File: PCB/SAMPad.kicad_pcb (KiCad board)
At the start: 2 copper layers, 73.2 x 116 mm, 162 parts, among them P1 USB_CONN, P1_2 USB_CONN, P4 CONN_6, P5 CONN_6, P6 ISP6, U1 ATMEGA32U4, U3 IP4234CZ6, U4 AP3417C, U5 PAM2804, X1 CRYSTAL

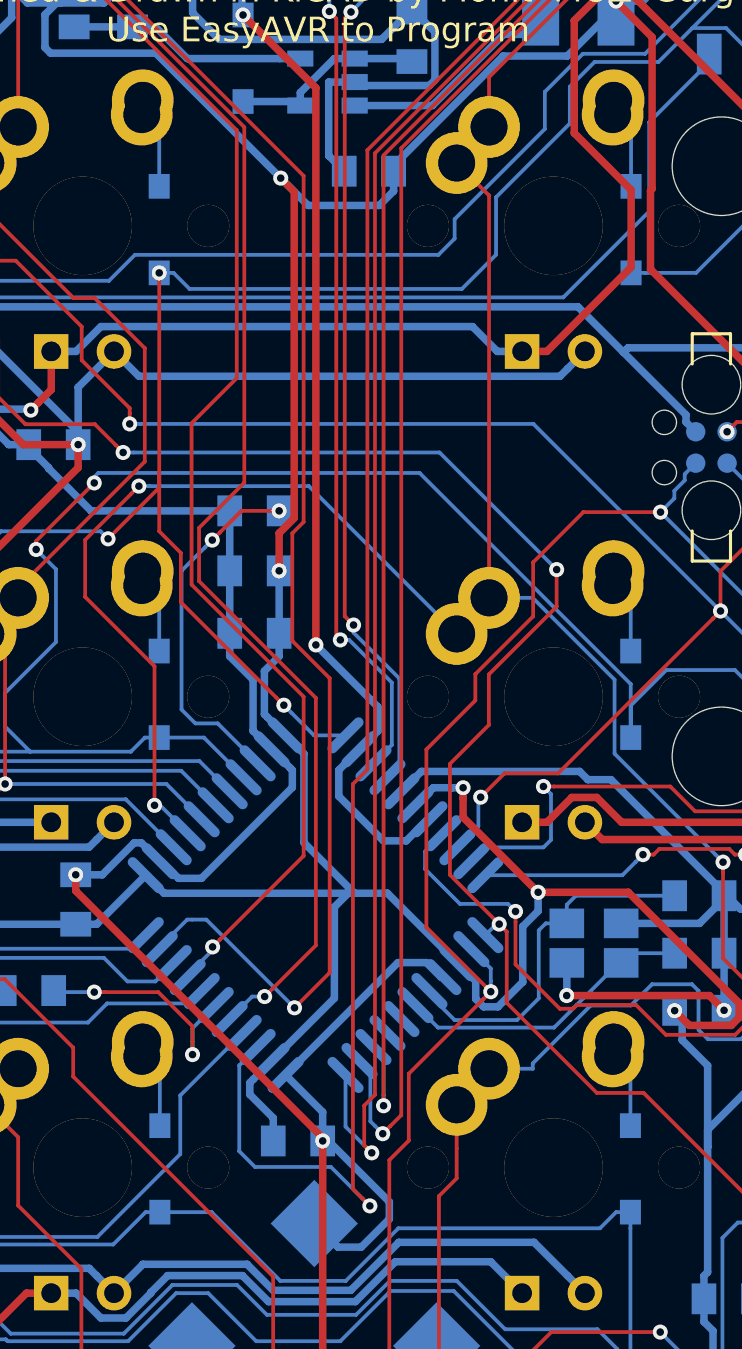
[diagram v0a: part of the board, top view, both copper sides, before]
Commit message: Fix Possible UVCC error
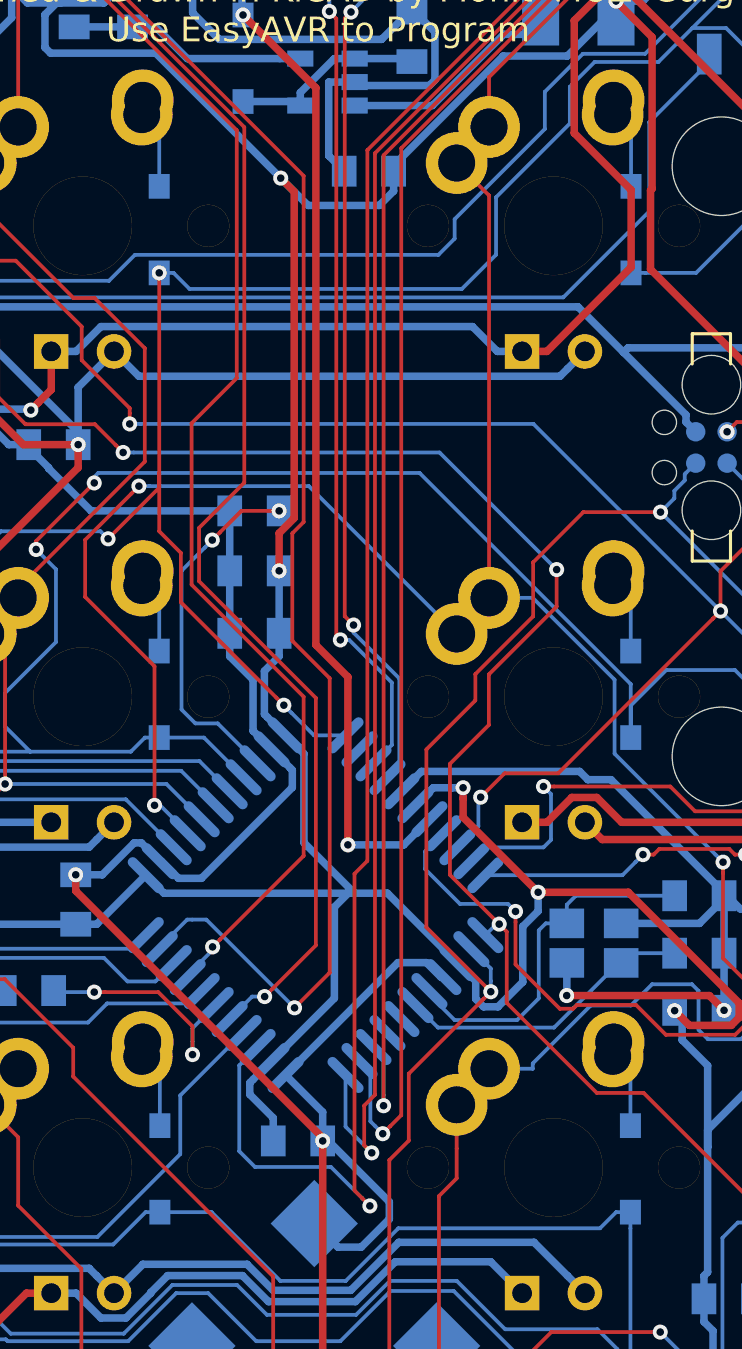
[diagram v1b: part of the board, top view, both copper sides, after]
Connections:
- U1 pad 2: /mcu/VUSB -> (no net)
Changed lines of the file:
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@@
 (kicad_pcb (version 4) (host pcbnew 4.0.1-stable)
   (general
-    (links 378)
-    (no_connects 0)
-    (area 90.373399 64.0226 166.776601 185.826601)
+    (links 377)
+    (no_connects 1)
+    (area 91.936499 68.123999 165.213501 184.263501)
     (thickness 1.6)
     (drawings 20)
-    (tracks 2085)
+    (tracks 2079)
     (zones 0)
     (modules 162)
@@
     (pad 3 smd oval (at -5.715 2.4003 225) (size 1.89992 0.4064) (layers B.Cu B.Mask)
       (net 75 /mcu/USB_D-))
-    (pad 2 smd oval (at -5.715 3.2004 225) (size 1.89992 0.4064) (layers B.Cu B.Mask)
-      (net 2 /mcu/VUSB))
+    (pad 2 smd oval (at -5.715 3.2004 225) (size 1.89992 0.4064) (layers B.Cu B.Mask))
     (pad 32 smd oval (at 5.715 3.2004 225) (size 1.89992 0.4064) (layers B.Cu B.Mask)
       (net 10 /mcu/ROW1))
@@
   (segment (start 127.1526 102.0953) (end 123.5 105.7479) (width 0.3048) (layer B.Cu) (net 1))
   (segment (start 123.5 105.7479) (end 123.5 105.9053) (width 0.3048) (layer B.Cu) (net 1))
+  (segment (start 129.7813 144.0942) (end 132.043112 144.0942) (width 0.3048) (layer B.Cu) (net 2))
+  (segment (start 132.043112 144.0942) (end 133.080071 143.057241) (width 0.3048) (layer B.Cu) (net 2))
+  (segment (start 128.48591 136.0043) (end 129.7813 137.29969) (width 0.3048) (layer F.Cu) (net 2))
+  (segment (start 129.7813 137.29969) (end 129.7813 144.0942) (width 0.3048) (layer F.Cu) (net 2))
+  (via (at 129.7813 144.0942) (size 0.6096) (drill 0.3048) (layers F.Cu B.Cu) (net 2))
   (segment (start 115.951 99.7204) (end 118.364 97.3074) (width 0.3048) (layer B.Cu) (net 2))
   (segment (start 118.364 97.3074) (end 118.364 95.2754) (width 0.3048) (layer B.Cu) (net 2))
@@
   (segment (start 125.5 105.2717) (end 126.238 104.5337) (width 0.3048) (layer B.Cu) (net 2))
   (via (at 126.238 104.5337) (size 0.6096) (drill 0.3048) (layers F.Cu B.Cu) (net 2))
-  (segment (start 133.080071 143.057241) (end 133.015359 143.057241) (width 0.3048) (layer B.Cu) (net 2))
-  (segment (start 133.015359 143.057241) (end 132.1435 143.9291) (width 0.3048) (layer B.Cu) (net 2))
-  (segment (start 132.1435 143.9291) (end 131.2164 143.9291) (width 0.3048) (layer B.Cu) (net 2))
-  (segment (start 131.2164 143.9291) (end 129.413 142.1257) (width 0.3048) (layer B.Cu) (net 2))
-  (segment (start 129.413 142.1257) (end 129.413 141.066751) (width 0.3048) (layer B.Cu) (net 2))
-  (segment (start 129.413 141.066751) (end 130.251291 140.22846) (width 0.3048) (layer B.Cu) (net 2))
   (segment (start 128.48591 136.0043) (end 128.48591 113.46689) (width 0.3048) (layer F.Cu) (net 2))
   (segment (start 128.48591 113.46689) (end 125.5395 110.52048) (width 0.3048) (layer F.Cu) (net 2))
   (via (at 125.5395 110.52048) (size 0.6096) (drill 0.3048) (layers F.Cu B.Cu) (net 2))
-  (segment (start 130.251291 140.22846) (end 130.993724 139.486027) (width 0.3048) (layer B.Cu) (net 2))
-  (segment (start 130.993724 139.486027) (end 130.993724 138.512114) (width 0.3048) (layer B.Cu) (net 2))
-  (segment (start 130.993724 138.512114) (end 130.720811 138.239201) (width 0.3048) (layer B.Cu) (net 2))
-  (segment (start 130.720811 138.239201) (end 128.48591 136.0043) (width 0.3048) (layer B.Cu) (net 2))
-  (via (at 128.48591 136.0043) (size 0.6096) (drill 0.3048) (layers F.Cu B.Cu) (net 2))
   (segment (start 125.5 108.2548) (end 125.5 110.48098) (width 0.3048) (layer B.Cu) (net 2))
   (segment (start 125.5 110.48098) (end 125.5395 110.52048) (width 0.3048) (layer B.Cu) (net 2))
@@
   (segment (start 115.0874 81.2513) (end 117.7638 81.2513) (width 0.1524) (layer B.Cu) (net 58))
   (segment (start 117.7638 81.2513) (end 117.78 81.2675) (width 0.1524) (layer B.Cu) (net 58))
-  (segment (start 126.022101 157.124401) (end 129.095501 157.124401) (width 0.1524) (layer B.Cu) (net 59))
-  (segment (start 125.38692 156.48922) (end 126.022101 157.124401) (width 0.1524) (layer B.Cu) (net 59))
   (segment (start 139.37 81.2675) (end 138.06171 79.95921) (width 0.1524) (layer F.Cu) (net 59))
+  (segment (start 147.43432 73.13932) (end 147.43432 90.307192) (width 0.1524) (layer F.Cu) (net 59))
   (segment (start 138.06171 79.95921) (end 133.759697 79.95921) (width 0.1524) (layer F.Cu) (net 59))
-  (segment (start 126.129353 152.270984) (end 125.38692 153.013417) (width 0.1524) (layer B.Cu) (net 59))
   (segment (start 129.54 72.1487) (end 130.2004 71.4883) (width 0.1524) (layer F.Cu) (net 59))
-  (segment (start 147.43432 73.13932) (end 147.43432 90.307192) (width 0.1524) (layer F.Cu) (net 59))
-  (segment (start 129.984501 158.013401) (end 130.365501 158.394401) (width 0.1524) (layer F.Cu) (net 59))
-  (segment (start 129.984501 141.632988) (end 129.984501 158.013401) (width 0.1524) (layer F.Cu) (net 59))
+  (segment (start 130.048 145.2626) (end 130.048 158.0769) (width 0.1524) (layer F.Cu) (net 59))
+  (segment (start 129.54 75.739513) (end 129.54 72.1487) (width 0.1524) (layer F.Cu) (net 59))
+  (segment (start 133.759697 79.95921) (end 129.54 75.739513) (width 0.1524) (layer F.Cu) (net 59))
+  (segment (start 130.2004 71.4883) (end 132.8166 71.4883) (width 0.1524) (layer F.Cu) (net 59))
+  (segment (start 130.048 158.0769) (end 130.365501 158.394401) (width 0.1524) (layer F.Cu) (net 59))
+  (segment (start 132.8166 71.4883) (end 134.676001 69.628899) (width 0.1524) (layer F.Cu) (net 59))
+  (segment (start 134.676001 69.628899) (end 143.923899 69.628899) (width 0.1524) (layer F.Cu) (net 59))
+  (segment (start 143.923899 69.628899) (end 147.43432 73.13932) (width 0.1524) (layer F.Cu) (net 59))
+  (segment (start 147.43432 90.307192) (end 147.180245 90.561267) (width 0.1524) (layer F.Cu) (net 59))
   (segment (start 147.180245 90.561267) (end 147.180245 99.377555) (width 0.1524) (layer F.Cu) (net 59))
   (segment (start 147.180245 99.377555) (end 130.568667 115.989133) (width 0.1524) (layer F.Cu) (net 59))
-  (segment (start 143.923899 69.628899) (end 147.43432 73.13932) (width 0.1524) (layer F.Cu) (net 59))
-  (segment (start 134.676001 69.628899) (end 143.923899 69.628899) (width 0.1524) (layer F.Cu) (net 59))
-  (segment (start 132.8166 71.4883) (end 134.676001 69.628899) (width 0.1524) (layer F.Cu) (net 59))
+  (segment (start 130.568667 144.741933) (end 130.048 145.2626) (width 0.1524) (layer F.Cu) (net 59))
+  (segment (start 130.568667 115.989133) (end 130.568667 144.741933) (width 0.1524) (layer F.Cu) (net 59))
   (segment (start 130.365501 158.394401) (end 130.6703 158.6992) (width 0.1524) (layer F.Cu) (net 59))
-  (segment (start 133.759697 79.95921) (end 129.54 75.739513) (width 0.1524) (layer F.Cu) (net 59))
-  (segment (start 130.568667 115.989133) (end 130.568667 141.048822) (width 0.1524) (layer F.Cu) (net 59))
+  (segment (start 126.022101 157.124401) (end 129.095501 157.124401) (width 0.1524) (layer B.Cu) (net 59))
+  (segment (start 125.38692 156.48922) (end 126.022101 157.124401) (width 0.1524) (layer B.Cu) (net 59))
+  (segment (start 126.129353 152.270984) (end 125.38692 153.013417) (width 0.1524) (layer B.Cu) (net 59))
   (via (at 130.6703 158.6992) (size 0.6096) (drill 0.3048) (layers F.Cu B.Cu) (net 59))
   (segment (start 125.38692 153.013417) (end 125.38692 156.48922) (width 0.1524) (layer B.Cu) (net 59))
-  (segment (start 129.54 75.739513) (end 129.54 72.1487) (width 0.1524) (layer F.Cu) (net 59))
   (segment (start 130.365501 158.394401) (end 130.6703 158.6992) (width 0.1524) (layer B.Cu) (net 59))
-  (segment (start 130.2004 71.4883) (end 132.8166 71.4883) (width 0.1524) (layer F.Cu) (net 59))
   (segment (start 129.095501 157.124401) (end 130.365501 158.394401) (width 0.1524) (layer B.Cu) (net 59))
-  (segment (start 130.568667 141.048822) (end 129.984501 141.632988) (width 0.1524) (layer F.Cu) (net 59))
-  (segment (start 147.43432 90.307192) (end 147.180245 90.561267) (width 0.1524) (layer F.Cu) (net 59))
   (segment (start 133.4262 81.1878) (end 136.7503 81.1878) (width 0.1524) (layer B.Cu) (net 60))
   (segment (start 136.7503 81.1878) (end 136.83 81.2675) (width 0.1524) (layer B.Cu) (net 60))

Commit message: Rev 0.2
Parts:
- moved HOLE1 0.19 mm to (128.1, 91.5)
- renumbered C19 to C6
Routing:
- net VSS: track 547.2 -> 537.2 mm, vias 12 -> 10
- net 3V3: track 490.4 -> 491.5 mm
- added copper zone on B.Cu, net VSS
- added copper zone on F.Cu, net VSS
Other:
- outline, holes or cut-outs redrawn
- board text added: "SAMPad Rev 0.2 Designed & Drawin in KiCAD by Mohit 'MOZ' Garg Use EasyAVR to Program"
- board text added: "SAMPad Rev 0.2 Designed & Drawn in KiCAD by Mohit 'MOZ' Garg Use EasyAVR to Program"
- board text removed: "SAMPad Rev 0.1 Designed & Drawin in KiCAD by Mohit 'MOZ' Garg Use EasyAVR to Program"
- board text removed: "SAMPad Rev 0.1 Designed & Drawn in KiCAD by Mohit 'MOZ' Garg Use EasyAVR to Program"
